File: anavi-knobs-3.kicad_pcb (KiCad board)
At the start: 2 copper layers, 35 x 81 mm, 10 parts, among them U1 SeeeduinoXIAO

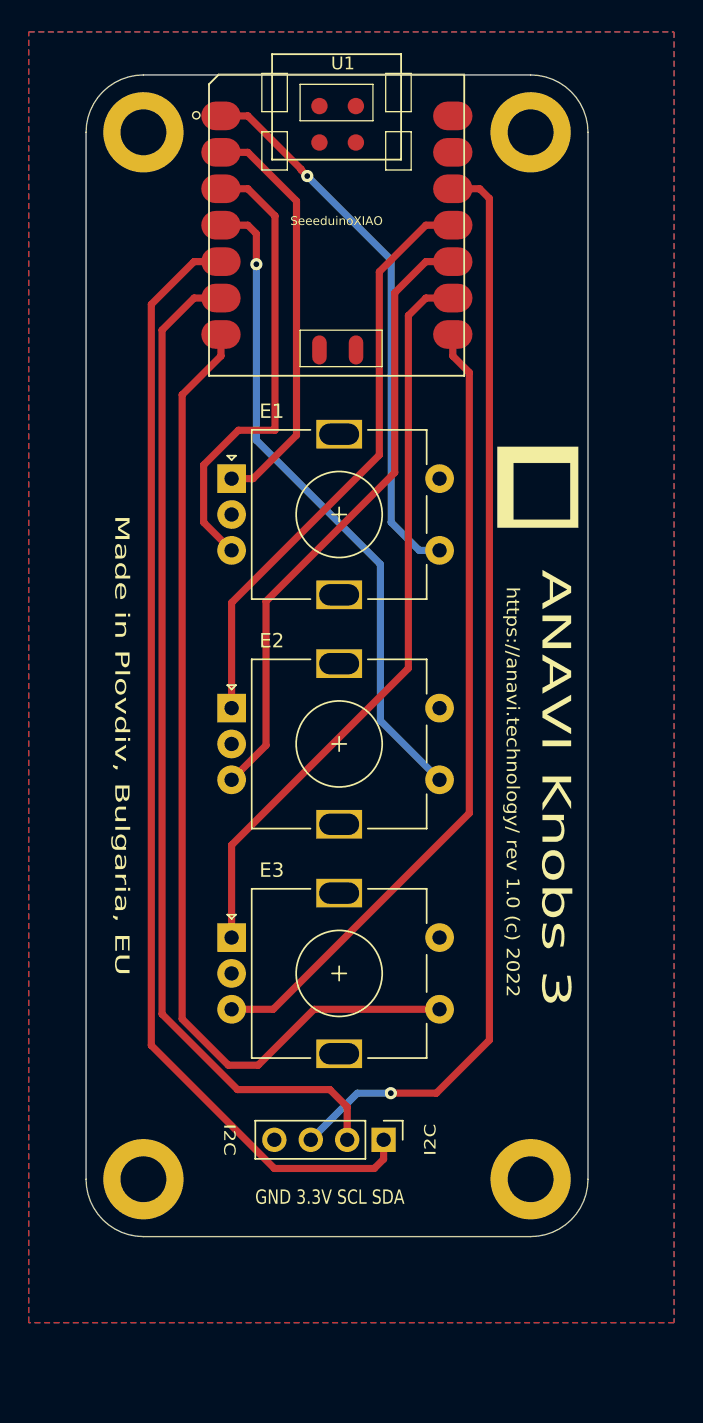
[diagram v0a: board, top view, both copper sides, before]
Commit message: anavi-knobs-3.kicad_pcb: Draw enclosure
Draw enclosure on the fabrication layer.

Signed-off-by: Leon Anavi <leon@anavi.org>
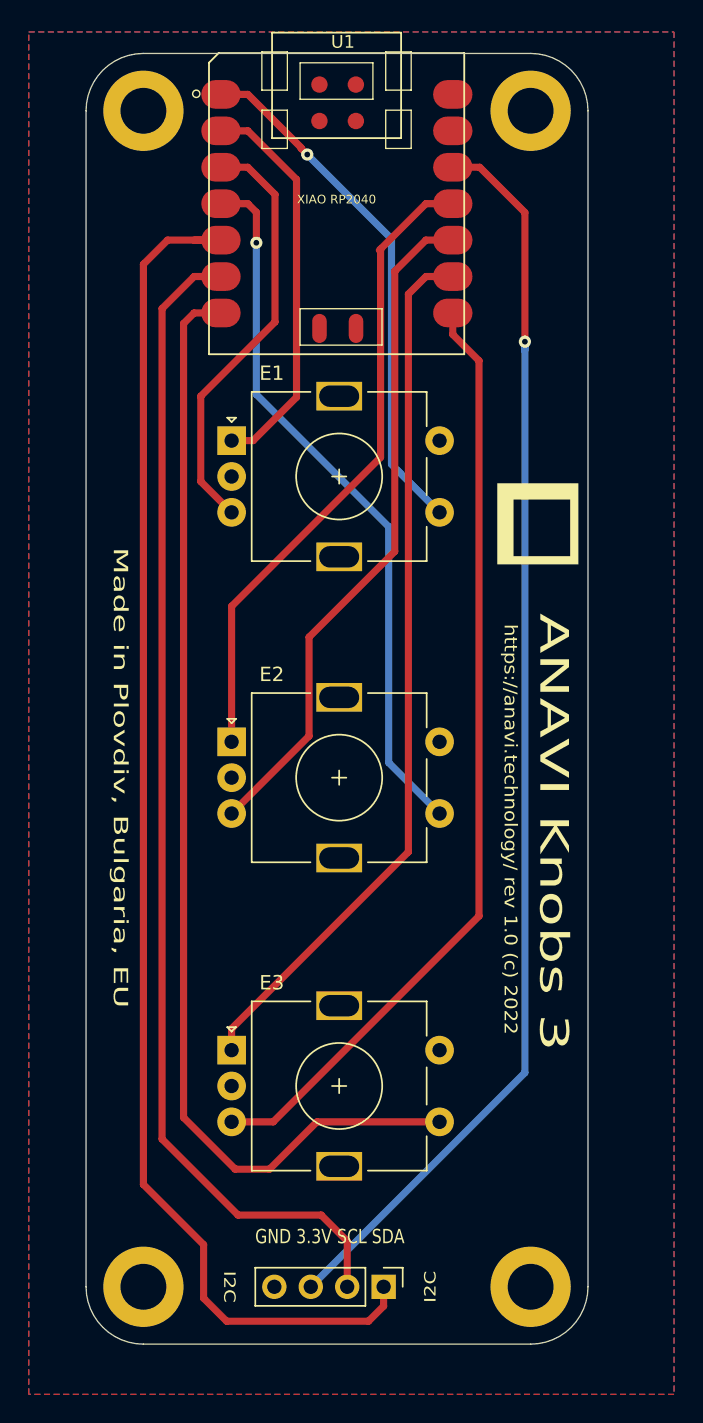
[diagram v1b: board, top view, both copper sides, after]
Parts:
- removed the REF** at (113.0, 125.0)
- removed the REF** at (140.0, 125.0)
- removed the REF** at (113.0, 52.0)
- removed the REF** at (140.0, 52.0)
- added REF**: MountingHole_3.2mm_M3_DIN965_Pad, MountingHole:MountingHole_3.2mm_M3_DIN965_Pad, F.Cu at (113.0, 132.5)
- added REF**: MountingHole_3.2mm_M3_DIN965_Pad, MountingHole:MountingHole_3.2mm_M3_DIN965_Pad, F.Cu at (140.0, 132.5)
- added REF**: MountingHole_3.2mm_M3_DIN965_Pad, MountingHole:MountingHole_3.2mm_M3_DIN965_Pad, F.Cu at (113.0, 50.5)
- added REF**: MountingHole_3.2mm_M3_DIN965_Pad, MountingHole:MountingHole_3.2mm_M3_DIN965_Pad, F.Cu at (140.0, 50.5)
- U1: value SeeeduinoXIAO -> XIAO RP2040
- moved I2C 10.2 mm to (129.8, 132.5)
- moved E3 7.85 mm to (119.2, 116.0)
- moved E1 2.65 mm to (119.2, 73.5)
- moved G*** 2.55 mm to (140.5, 79.3)
- moved E2 2.35 mm to (119.2, 94.5)
- moved U1 1.50 mm to (117.6, 67.5)
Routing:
- net Net-(J1-Pad1): track 79.1 -> 97.2 mm
- net +3V3: track 76.9 -> 88.6 mm
- net Net-(J1-Pad2): track 70.6 -> 82.0 mm
- net Net-(E3-PadB): track 56.1 -> 66.0 mm
- net Net-(E3-PadA): track 52.1 -> 61.4 mm
- net Net-(E3-PadS1): track 69.8 -> 79.0 mm
- net Net-(E2-PadA): track 41.2 -> 45.1 mm
- net Net-(E2-PadB): track 43.6 -> 47.5 mm
- net Net-(E2-PadS1): track 46.1 -> 49.9 mm
- net Net-(E1-PadB): track 32.2 -> 29.8 mm
- net Net-(E1-PadS1): track 38.5 -> 36.6 mm
- net Net-(E1-PadA): track 28.8 -> 27.6 mm
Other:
- board size 35 x 81 mm -> 35 x 90 mm
